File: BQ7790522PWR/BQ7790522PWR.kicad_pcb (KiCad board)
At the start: 2 copper layers, 40 x 34 mm, 53 parts, among them J1 BAT, J2 BAT_NEG, J3 DSG, J4 LDU, J5 LOAD_NEG, J6 TS, J7 CTRD, J8 CTRC, J9 CHGU, Q1 IAUC41N06S5N102ATMA1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

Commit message: update schematic and pcb
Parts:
- removed Q1, Q2: IAUC41N06S5N102ATMA1, BQ7790522PWR:IAUC41N06S5N102
- added U2: SIR172ADP-T1-GE3, Package_SO:PowerPAK_SO-8_Single, F.Cu at (41.7, 45.4)
- added U3: SIR172ADP-T1-GE3, Package_SO:PowerPAK_SO-8_Single, F.Cu at (50.8, 45.4)
- R23, R24: value 0 -> 1k
- moved C11 0.25 mm to (52.5, 49.4)
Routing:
- net /B_OUT: track 13.2 -> 11.9 mm, vias 6 -> 8
- net /SW_IN: track 11.1 -> 9.94 mm, vias 12 -> 13
- net Net-(R10-Pad2): track 16.9 -> 16.1 mm
- net /SW_C: vias 16 -> 22
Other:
- board size 40 x 34 mm -> 40 x 35 mm
- board text added: "3 cells: B5 + B4 + B3 shorted"
- board text added: "4 cells: B5 + B4 shorted"
- board text added: "CHGU"
- board text added: "CTRC"
- board text added: "CTRD"
- board text added: "DSG"
- board text added: "LDU"
- board text added: "NTC"

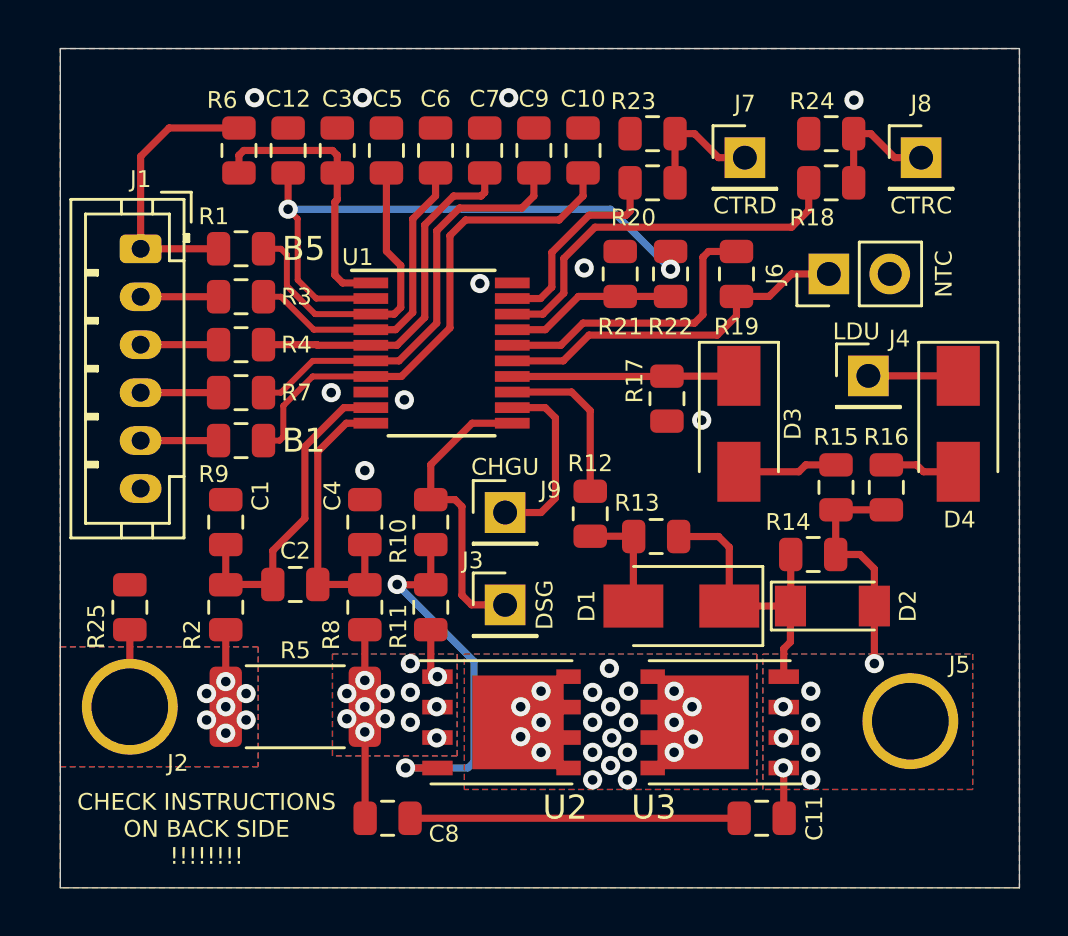
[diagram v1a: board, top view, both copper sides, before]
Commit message: create interactive BOM and order all parts
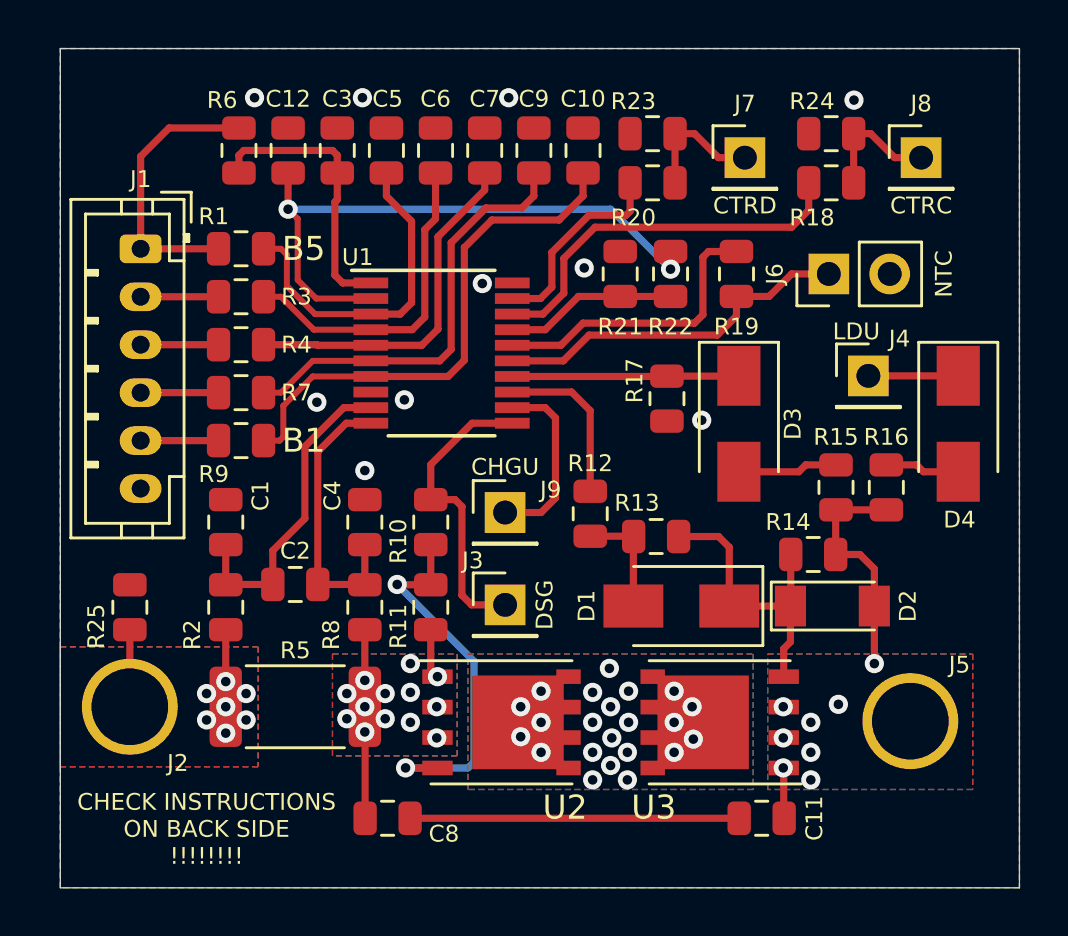
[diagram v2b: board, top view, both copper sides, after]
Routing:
- net /VC5: track 13.6 -> 14.1 mm
